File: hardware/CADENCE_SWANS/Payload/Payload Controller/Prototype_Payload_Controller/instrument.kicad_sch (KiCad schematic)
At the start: 1 part, among them J1 Conn_01x06_Pin

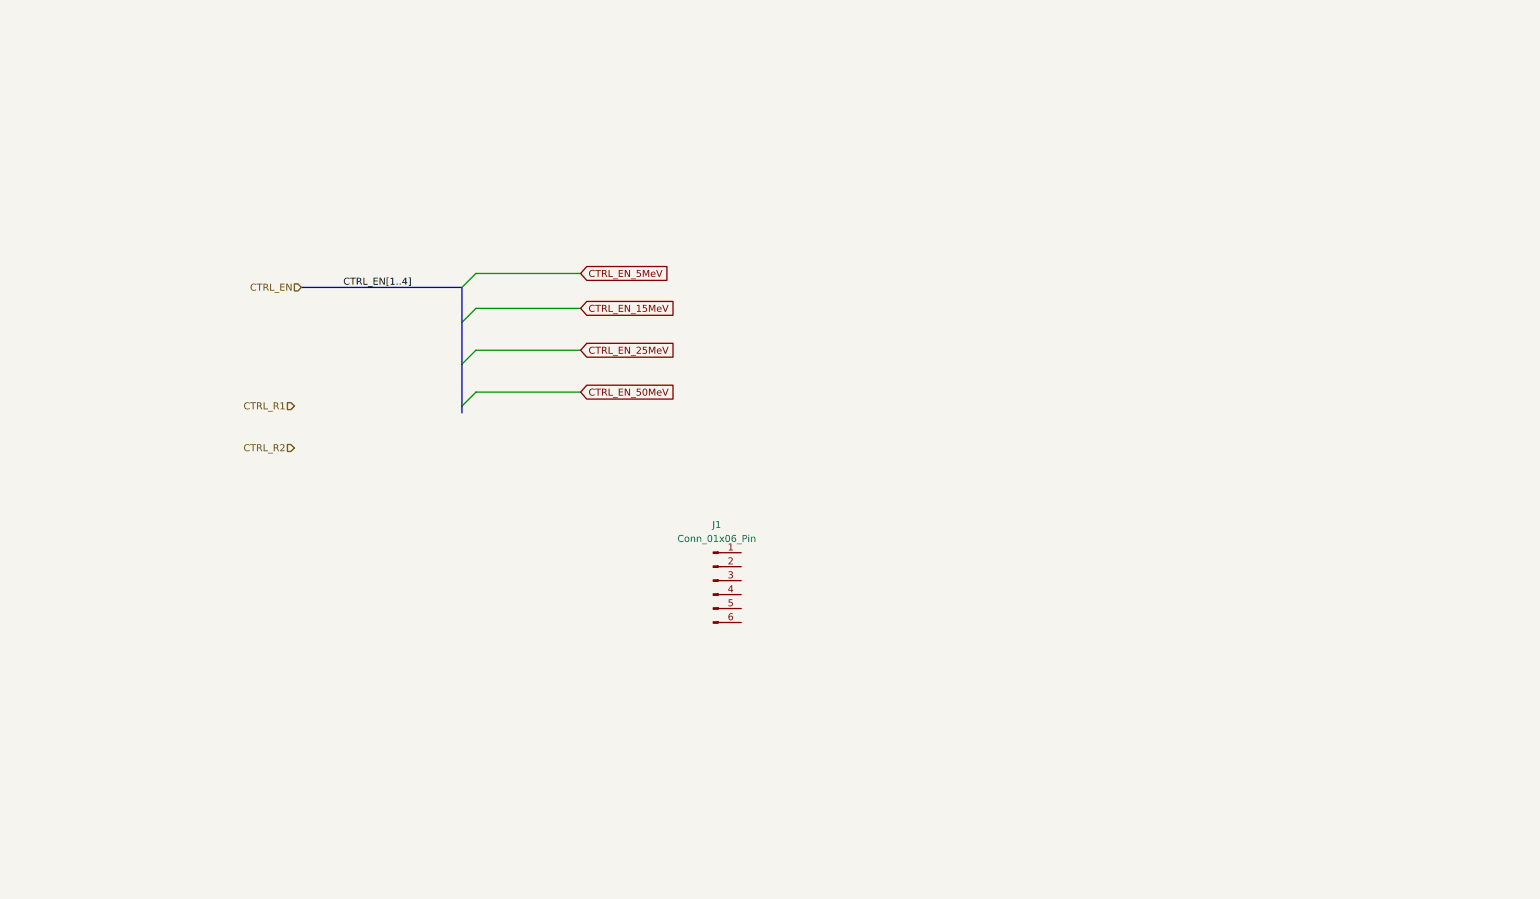
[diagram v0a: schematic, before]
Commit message: Instrument.sch updates
Added Control Readout module, and made it more legible and clean
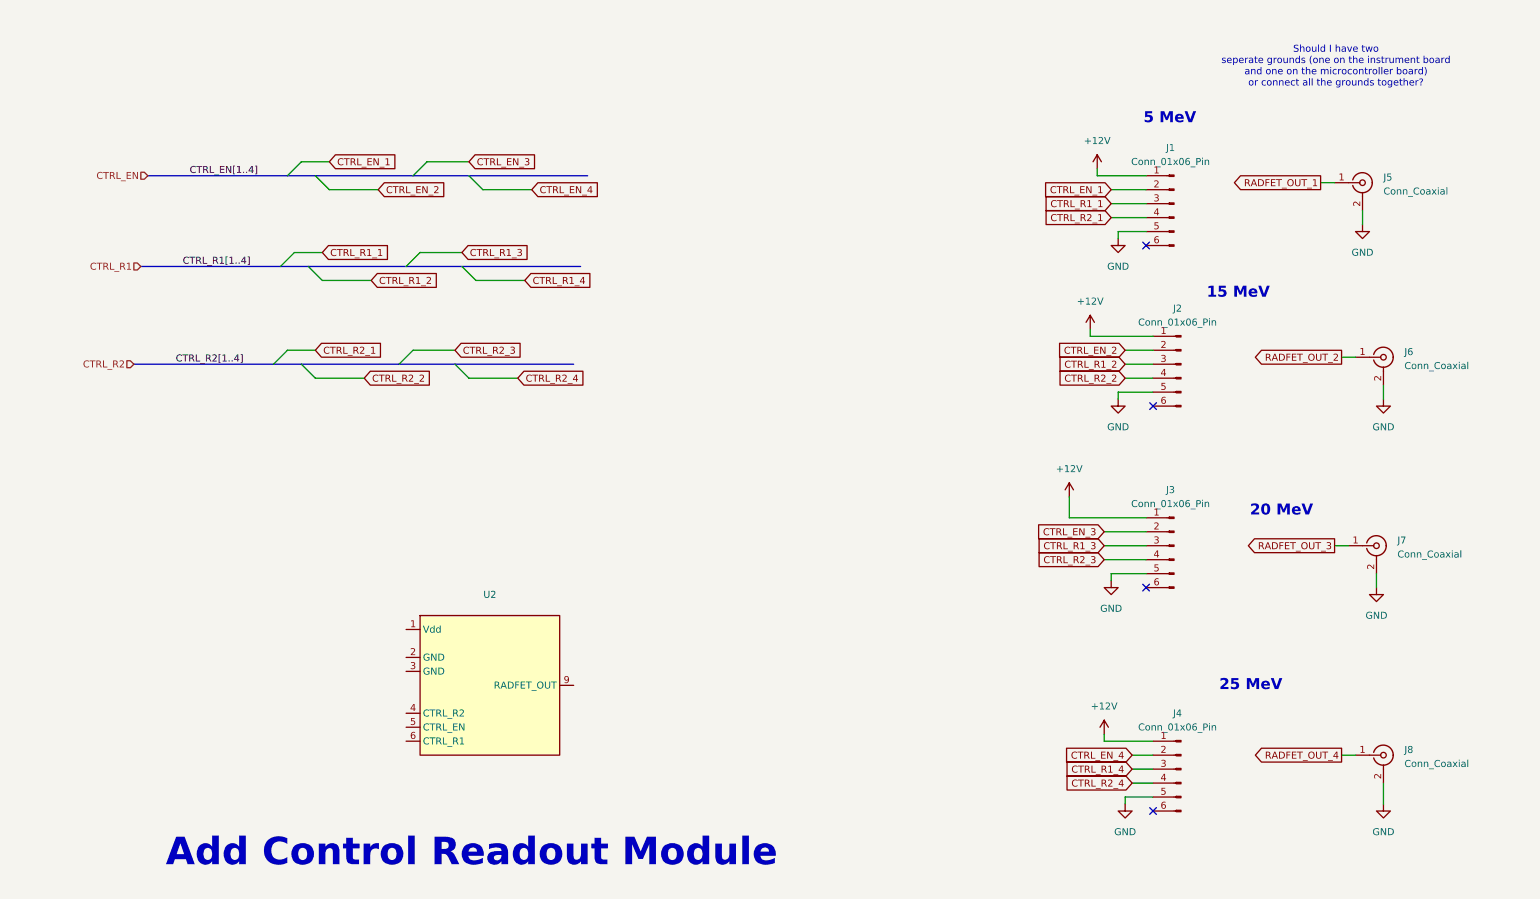
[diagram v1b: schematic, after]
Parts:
- added J2, J3, J4: Conn_01x06_Pin, symbol Connector:Conn_01x06_Pin
- added J5, J6, J7, J8: Conn_Coaxial, symbol Connector:Conn_Coaxial
- added U2: ~, symbol VT01-RM:RM_VT01_A_RADFET Readout Module
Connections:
- net +12V: now reaches J1.1 (Pin_1)
- net +12V: now also J2.1 (Pin_1), J3.1 (Pin_1), J4.1 (Pin_1)
- net CTRL_EN_1: now reaches J1.2 (Pin_2)
- net CTRL_R1_1: now reaches J1.3 (Pin_3)
- net CTRL_R2_1: now reaches J1.4 (Pin_4)
- net GND: now reaches J1.5 (Pin_5)
- net GND: now also J2.5 (Pin_5), J3.5 (Pin_5), J4.5 (Pin_5), J5.2 (Ext), J6.2 (Ext), J7.2 (Ext), J8.2 (Ext)
- new net CTRL_EN_2: J2.2 (Pin_2)
- new net CTRL_EN_3: J3.2 (Pin_2)
- new net CTRL_EN_4: J4.2 (Pin_2)
- new net CTRL_R1_2: J2.3 (Pin_3)
- new net CTRL_R1_3: J3.3 (Pin_3)
- new net CTRL_R1_4: J4.3 (Pin_3)
- new net CTRL_R2_2: J2.4 (Pin_4)
- new net CTRL_R2_3: J3.4 (Pin_4)
- new net CTRL_R2_4: J4.4 (Pin_4)
- new net RADFET_OUT_1: J5.1 (In)
- new net RADFET_OUT_2: J6.1 (In)
- new net RADFET_OUT_3: J7.1 (In)
- new net RADFET_OUT_4: J8.1 (In)
- no-connect marks 0 -> 4
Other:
- note added: "15 MeV"
- note added: "20 MeV"
- note added: "25 MeV"
- note added: "5 MeV"
- note added: "Add Control Readout Module"
- note added: "Should I have two seperate grounds (one on the instrument board and one on the microcontroller board) or connect all the grounds together?"
- moved on the sheet: J1

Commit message: Updates
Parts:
- added C1: 10uF, symbol Device:C_Small
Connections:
- net +12V: now also U2.1 (Vdd), C1.1
- net GND: now also U2.2 (GND), U2.3 (GND), C1.2
- net CTRL_EN_0: now reaches U2.4 (CTRL_R2)
- net CTRL_R1_0: now reaches U2.5 (CTRL_EN)
- net CTRL_R2_0: now reaches U2.6 (CTRL_R1)
- net RADFET_OUT_0: now reaches U2.9 (RADFET_OUT)
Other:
- note added: "Control Readout Module"
- note added: "MCU Control Signals"
- note removed: "Add Control Readout Module"
- moved on the sheet: J1, J2, J5, J6, U2

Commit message: updates
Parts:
- added J10: Conn_01x03, symbol Connector_Generic:Conn_01x03
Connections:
- net +12V: now also J10.1 (Pin_1); no longer C1.1, J1.1 (Pin_1), J2.1 (Pin_1), J3.1 (Pin_1), J4.1 (Pin_1), U2.1 (Vdd)
- new net VBAT: J10.3 (Pin_3)
- new net VDD: C1.1, J1.1 (Pin_1), J10.2 (Pin_2), J2.1 (Pin_1), J3.1 (Pin_1), J4.1 (Pin_1), U2.1 (Vdd)
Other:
- note removed: "Should I have two seperate grounds (one on the instrument board and one on the microcontroller board) or connect all the grounds together?"

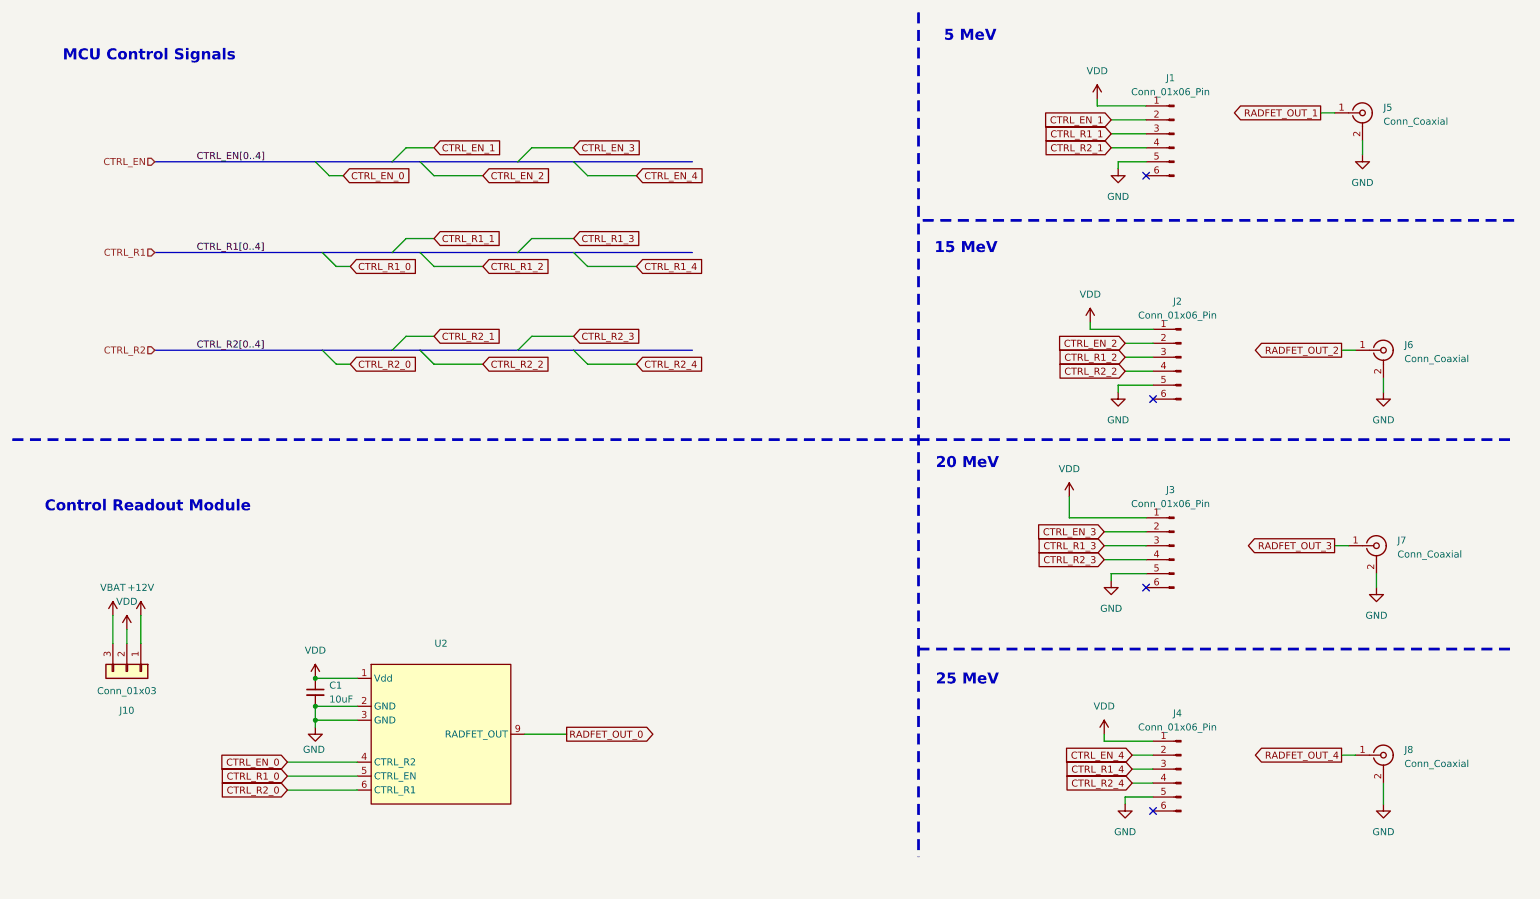
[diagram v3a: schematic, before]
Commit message: updated net labels
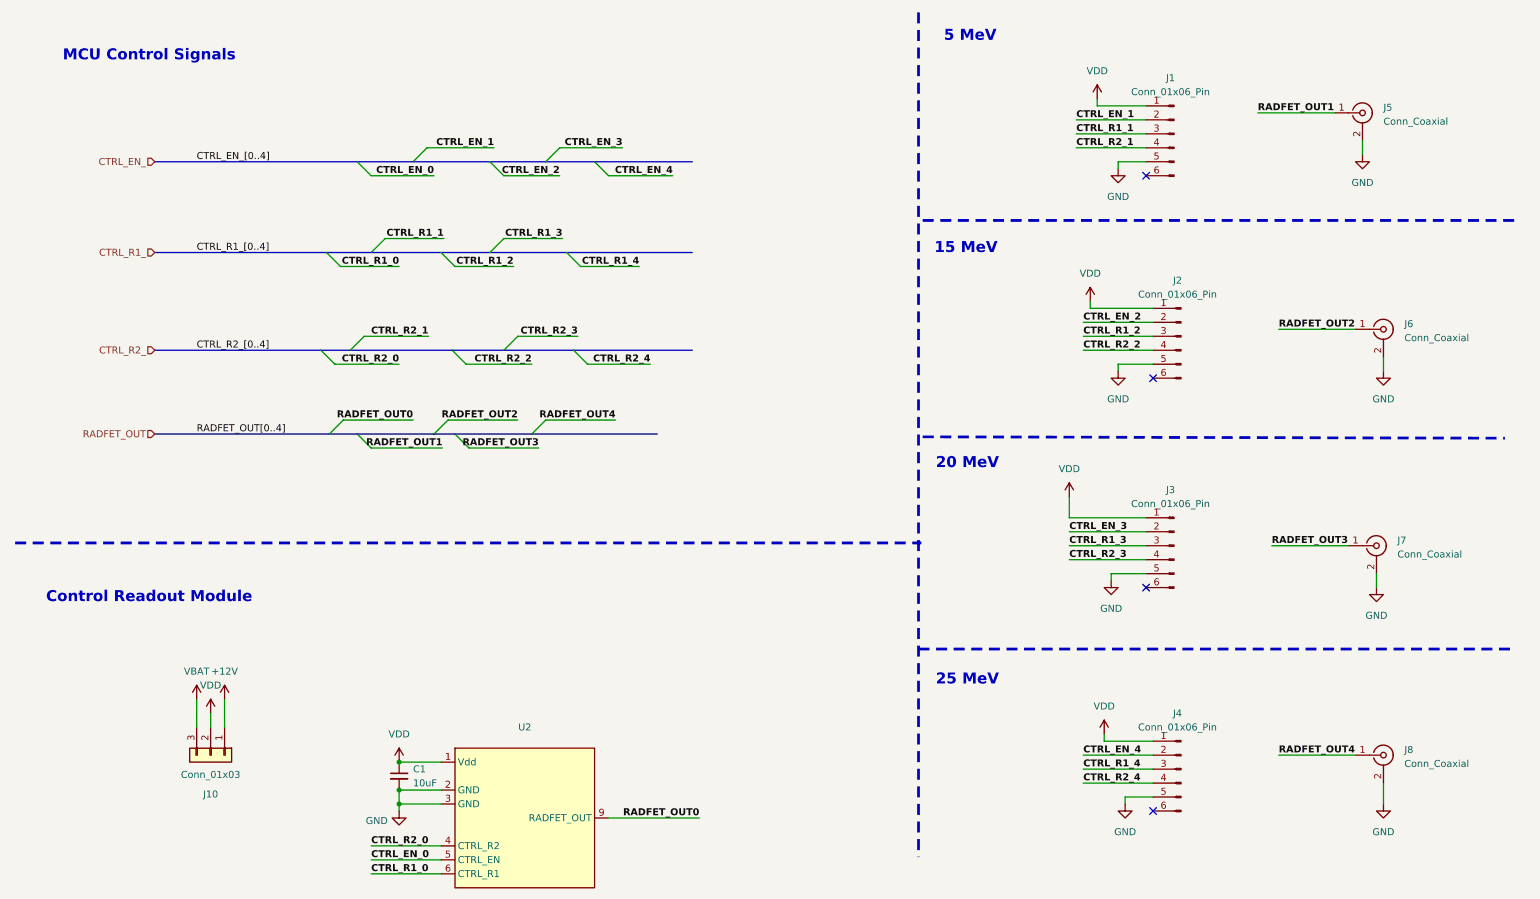
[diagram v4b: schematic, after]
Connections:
- net CTRL_EN_0: now also U2.5 (CTRL_EN); no longer U2.4 (CTRL_R2)
- net CTRL_R1_0: now also U2.6 (CTRL_R1); no longer U2.5 (CTRL_EN)
- net CTRL_R2_0: now also U2.4 (CTRL_R2); no longer U2.6 (CTRL_R1)
- net RADFET_OUT_0 renamed RADFET_OUT0
- net RADFET_OUT_1 renamed RADFET_OUT1
- net RADFET_OUT_2 renamed RADFET_OUT2
- net RADFET_OUT_3 renamed RADFET_OUT3
- net RADFET_OUT_4 renamed RADFET_OUT4
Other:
- moved on the sheet: C1, J10, J2, J6, U2

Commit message: updated MRAM Schematic Symbol
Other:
- moved on the sheet: C1, U2
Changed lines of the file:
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@@
 	)
 	(junction
-		(at 82.55 156.21)
+		(at 83.82 156.21)
 		(diameter 0)
 		(color 0 0 0 0)
 	)
 	(junction
-		(at 82.55 153.67)
+		(at 83.82 153.67)
 		(diameter 0)
 		(color 0 0 0 0)
 	)
 	(junction
-		(at 82.55 148.59)
+		(at 83.82 148.59)
 		(diameter 0)
 		(color 0 0 0 0)
@@
 	(wire
 		(pts
-			(xy 82.55 153.67) (xy 90.17 153.67)
+			(xy 83.82 153.67) (xy 91.44 153.67)
 		)
 		(stroke
@@
 	(wire
 		(pts
-			(xy 77.47 166.37) (xy 90.17 166.37)
+			(xy 78.74 166.37) (xy 91.44 166.37)
 		)
 		(stroke
@@
 	(wire
 		(pts
-			(xy 82.55 153.67) (xy 82.55 156.21)
+			(xy 83.82 153.67) (xy 83.82 156.21)
 		)
 		(stroke
@@
 	(wire
 		(pts
-			(xy 82.55 156.21) (xy 82.55 157.48)
+			(xy 83.82 156.21) (xy 83.82 157.48)
 		)
 		(stroke
@@
 	(wire
 		(pts
-			(xy 77.47 163.83) (xy 90.17 163.83)
+			(xy 78.74 163.83) (xy 91.44 163.83)
 		)
 		(stroke
@@
 	(wire
 		(pts
-			(xy 82.55 156.21) (xy 90.17 156.21)
+			(xy 83.82 156.21) (xy 91.44 156.21)
 		)
 		(stroke
@@
 	(wire
 		(pts
-			(xy 82.55 148.59) (xy 90.17 148.59)
+			(xy 83.82 148.59) (xy 91.44 148.59)
 		)
 		(stroke
@@
 	(wire
 		(pts
-			(xy 120.65 158.75) (xy 137.16 158.75)
+			(xy 121.92 158.75) (xy 138.43 158.75)
 		)
 		(stroke
@@
 	(wire
 		(pts
-			(xy 77.47 168.91) (xy 90.17 168.91)
+			(xy 78.74 168.91) (xy 91.44 168.91)
 		)
 		(stroke
@@
 	)
 	(label "CTRL_R2_0"
-		(at 77.47 163.83 0)
+		(at 78.74 163.83 0)
 		(effects
 			(font
@@
 	)
 	(label "CTRL_EN_0"
-		(at 77.47 166.37 0)
+		(at 78.74 166.37 0)
 		(effects
 			(font
@@
 	)
 	(label "CTRL_R1_0"
-		(at 77.47 168.91 0)
+		(at 78.74 168.91 0)
 		(effects
 			(font
@@
 	)
 	(label "RADFET_OUT0"
-		(at 137.16 158.75 180)
+		(at 138.43 158.75 180)
 		(effects
 			(font
@@
 	)
 	(hierarchical_label "RADFET_OUT"
-		(shape input)
+		(shape output)
 		(at 38.1 88.9 180)
 		(effects
@@
 	(symbol
 		(lib_id "Device:C_Small")
-		(at 82.55 151.13 0)
+		(at 83.82 151.13 0)
 		(unit 1)
 		(exclude_from_sim no)
@@
 		(dnp no)
 		(property "Reference" "C1"
-			(at 85.09 149.8662 0)
+			(at 86.36 149.8662 0)
 			(effects
 				(font
@@
 		)
 		(property "Value" "10uF"
-			(at 85.09 152.4 0)
+			(at 86.36 152.4 0)
 			(effects
 				(font
@@
 		)
 		(property "Footprint" ""
-			(at 82.55 151.13 0)
+			(at 83.82 151.13 0)
 			(effects
 				(font
@@
 		)
 		(property "Datasheet" "~"
-			(at 82.55 151.13 0)
+			(at 83.82 151.13 0)
 			(effects
 				(font
@@
 		)
 		(property "Description" "Unpolarized capacitor, small symbol"
-			(at 82.55 151.13 0)
+			(at 83.82 151.13 0)
 			(effects
 				(font
@@
 	(symbol
 		(lib_id "power:VDD")
-		(at 82.55 148.59 0)
+		(at 83.82 148.59 0)
 		(unit 1)
 		(exclude_from_sim no)
@@
 		(fields_autoplaced yes)
 		(property "Reference" "#PWR041"
-			(at 82.55 152.4 0)
+			(at 83.82 152.4 0)
 			(effects
 				(font
@@
 		)
 		(property "Value" "VDD"
-			(at 82.55 143.51 0)
+			(at 83.82 143.51 0)
 			(effects
 				(font
@@
 		)
 		(property "Footprint" ""
-			(at 82.55 148.59 0)
+			(at 83.82 148.59 0)
 			(effects
 				(font
@@
 		)
 		(property "Datasheet" ""
-			(at 82.55 148.59 0)
+			(at 83.82 148.59 0)
 			(effects
 				(font
@@
 		)
 		(property "Description" "Power symbol creates a global label with name \"VDD\""
-			(at 82.55 148.59 0)
+			(at 83.82 148.59 0)
 			(effects
 				(font
@@
 	(symbol
 		(lib_id "power:GND")
-		(at 82.55 157.48 0)
+		(at 83.82 157.48 0)
 		(unit 1)
 		(exclude_from_sim no)
@@
 		(dnp no)
 		(property "Reference" "#PWR013"
-			(at 82.55 163.83 0)
+			(at 83.82 163.83 0)
 			(effects
 				(font
@@
 		)
 		(property "Value" "GND"
-			(at 78.486 159.258 0)
+			(at 79.756 159.258 0)
 			(effects
 				(font
@@
 		)
 		(property "Footprint" ""
-			(at 82.55 157.48 0)
+			(at 83.82 157.48 0)
 			(effects
 				(font
@@
 		)
 		(property "Datasheet" ""
-			(at 82.55 157.48 0)
+			(at 83.82 157.48 0)
 			(effects
 				(font
@@
 		)
 		(property "Description" "Power symbol creates a global label with name \"GND\" , ground"
-			(at 82.55 157.48 0)
+			(at 83.82 157.48 0)
 			(effects
 				(font
@@
 	(symbol
 		(lib_id "VT01-RM:RM_VT01_A_RADFET Readout Module")
-		(at 92.71 171.45 0)
+		(at 93.98 171.45 0)
 		(unit 1)
 		(exclude_from_sim no)
@@
 		(on_board yes)
 		(dnp no)
-		(fields_autoplaced yes)
 		(property "Reference" "U2"
-			(at 105.41 142.24 0)
+			(at 106.426 143.256 0)
 			(effects
 				(font
@@
 		)
 		(property "Value" "~"
-			(at 105.41 144.78 0)
+			(at 106.68 144.78 0)
 			(effects
 				(font
@@
 		)
 		(property "Footprint" ""
-			(at 92.71 171.45 0)
+			(at 93.98 171.45 0)
 			(effects
 				(font
@@
 		)
 		(property "Datasheet" ""
-			(at 92.71 171.45 0)
+			(at 93.98 171.45 0)
 			(effects
 				(font
@@
 		)
 		(property "Description" ""
-			(at 92.71 171.45 0)
+			(at 93.98 171.45 0)
 			(effects
 				(font
